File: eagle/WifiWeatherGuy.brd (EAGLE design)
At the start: 70 x 43 mm, 4 parts

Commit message: ...
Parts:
- moved U$1 24.3 mm to (10.2, 49.5), turned to 0 degrees
- moved WEMOS1 5.08 mm to (41.9, 57.1), turned to 90 degrees
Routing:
- net N$6: track 13.3 -> 40.2 mm
- net N$4: track 31.6 -> 45.6 mm
- net N$3: track 37.4 -> 50.7 mm
- net N$7: track 50.3 -> 59.7 mm
- net N$2: track 32.7 -> 40.6 mm
- net N$9: track 34.7 -> 28.7 mm
- net N$8: track 33.6 -> 29.5 mm
- net N$1: track 47.4 -> 50.3 mm
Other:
- board text added: "SSID: WifiWeatherGuy Config: http://192.168.4.1"
- board text added: "WifiWeatherGuy #2 (c) 2017 Steve"
- board text removed: "(c) 2017 Steve"
- board text removed: "WifiWeatherGuy"

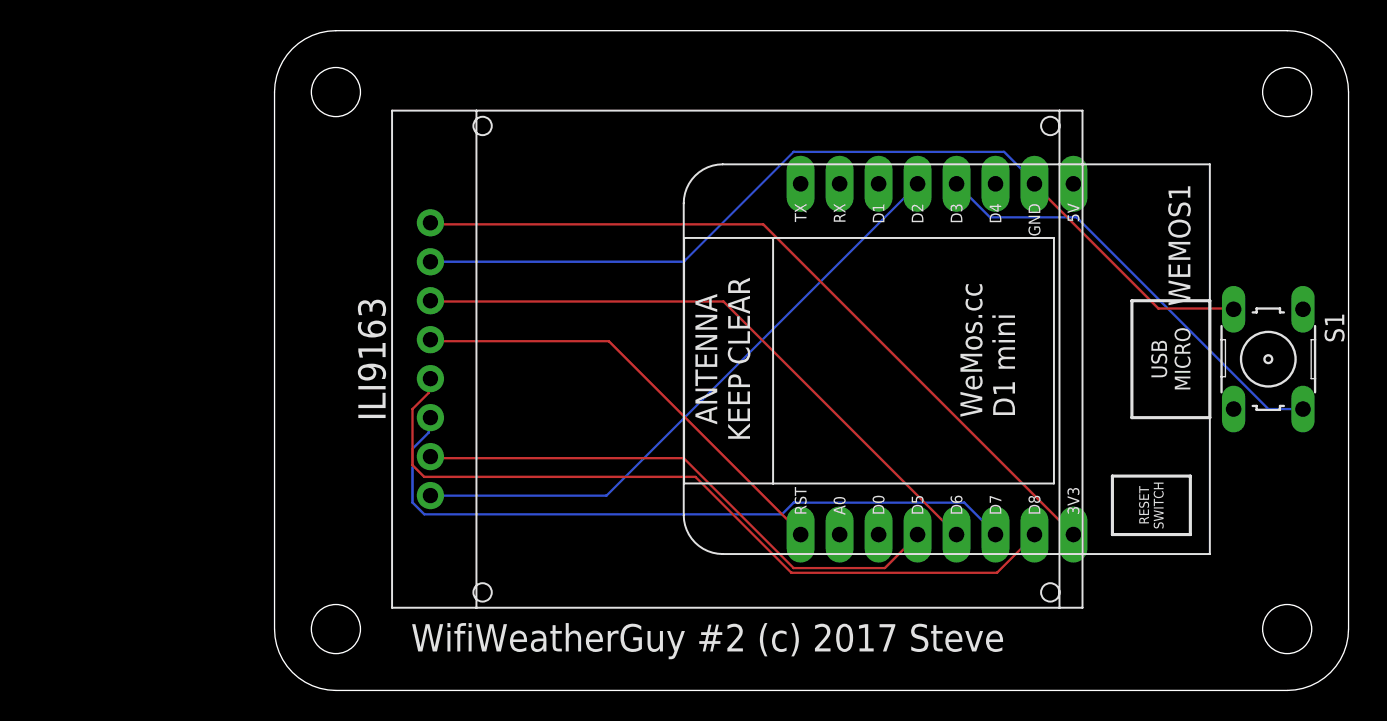
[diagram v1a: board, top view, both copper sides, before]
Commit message: add wemos pin headers
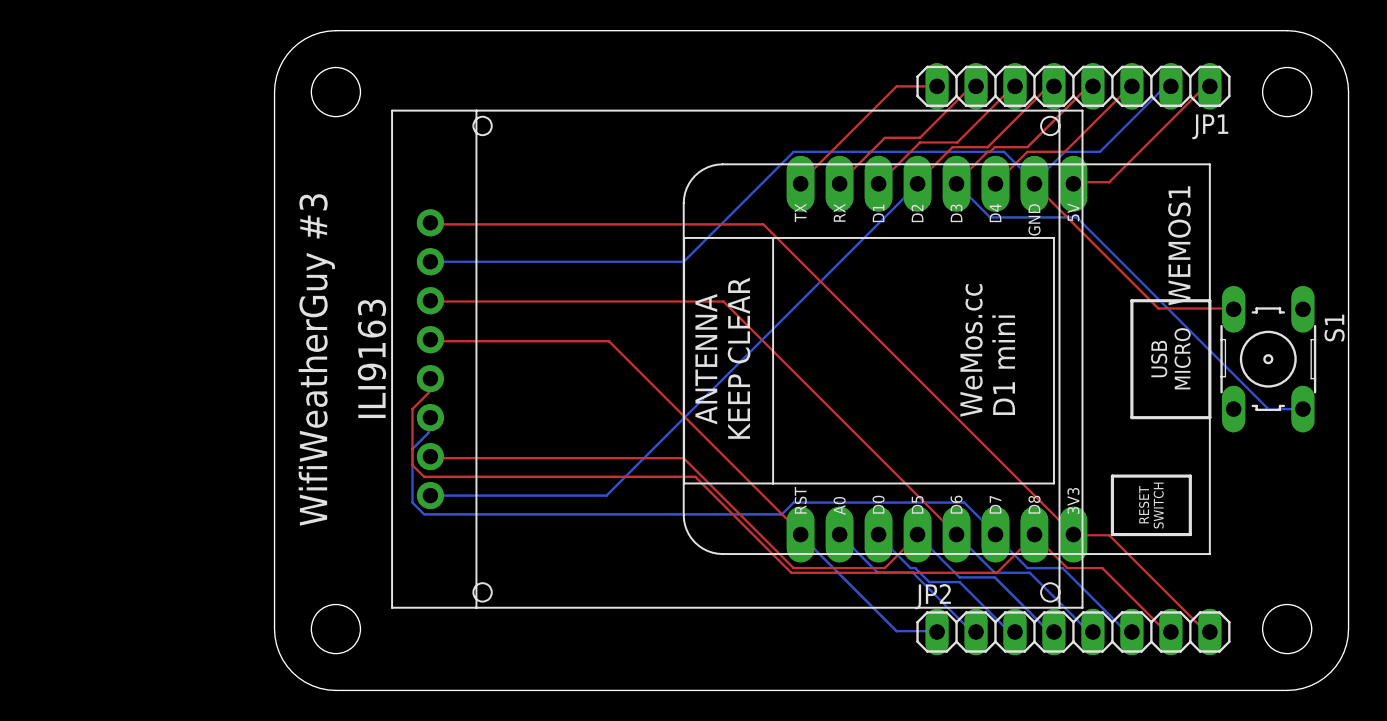
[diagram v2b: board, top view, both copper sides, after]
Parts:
- added JP1, JP2: (no value), pinhead:1X08
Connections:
- new net N$10: JP1.1, WEMOS1.5V
- new net N$11: JP1.3, WEMOS1.D4
- new net N$12: JP1.6, WEMOS1.D1
- new net N$13: JP1.7, WEMOS1.RX
- new net N$14: JP1.8, WEMOS1.TX
- new net N$15: JP2.2, WEMOS1.A0
- new net N$16: JP1.2, S1.3, U$1.GND, WEMOS1.GND
- net N$1: now also JP2.8
- net N$2: now also JP2.5
- net N$3: now also JP2.7
- net N$4: now also JP2.6
- net N$5: now also JP2.4
- net N$6: now also JP1.5
- net N$7: now also JP2.3, WEMOS1.D0; no longer S1.3, U$1.GND, WEMOS1.GND
- net N$8: now also JP2.1
- net N$9: now also JP1.4
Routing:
- net N$16: track 0.00 -> 71.1 mm
- net N$7: track 59.7 -> 11.6 mm
- net N$4: track 45.6 -> 57.2 mm
- net N$14: track 0.00 -> 11.6 mm
- net N$6: track 40.2 -> 51.8 mm
- net N$2: track 40.6 -> 52.2 mm
- net N$15: track 0.00 -> 11.6 mm
- net N$8: track 29.5 -> 41.0 mm
- net N$5: track 35.7 -> 47.3 mm
- net N$1: track 50.3 -> 61.9 mm
- net N$13: track 0.00 -> 11.5 mm
- net N$10: track 0.00 -> 11.5 mm
- net N$9: track 28.7 -> 40.2 mm
- net N$11: track 0.00 -> 11.5 mm
- net N$12: track 0.00 -> 11.5 mm
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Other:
- board text added: "SSID: WifiWeatherGuy Config: http://192.168.4.1 (c) 2018 Steve"
- board text added: "WifiWeatherGuy #3"
- board text removed: "SSID: WifiWeatherGuy Config: http://192.168.4.1"
- board text removed: "WifiWeatherGuy #2 (c) 2017 Steve"
